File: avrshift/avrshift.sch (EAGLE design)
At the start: 49 parts, among them IC1 AT90S2313P, IC2 7805TV, Q1 BC337-40, Q10 BC337-40, Q11 BC337-40, Q12 BC337-40, Q2 BC337-40, Q3 BC337-40, Q4 BC337-40, Q5 BC337-40, Q6 BC337-40, Q7 BC337-40, Q8 BC337-40, Q9 BC337-40

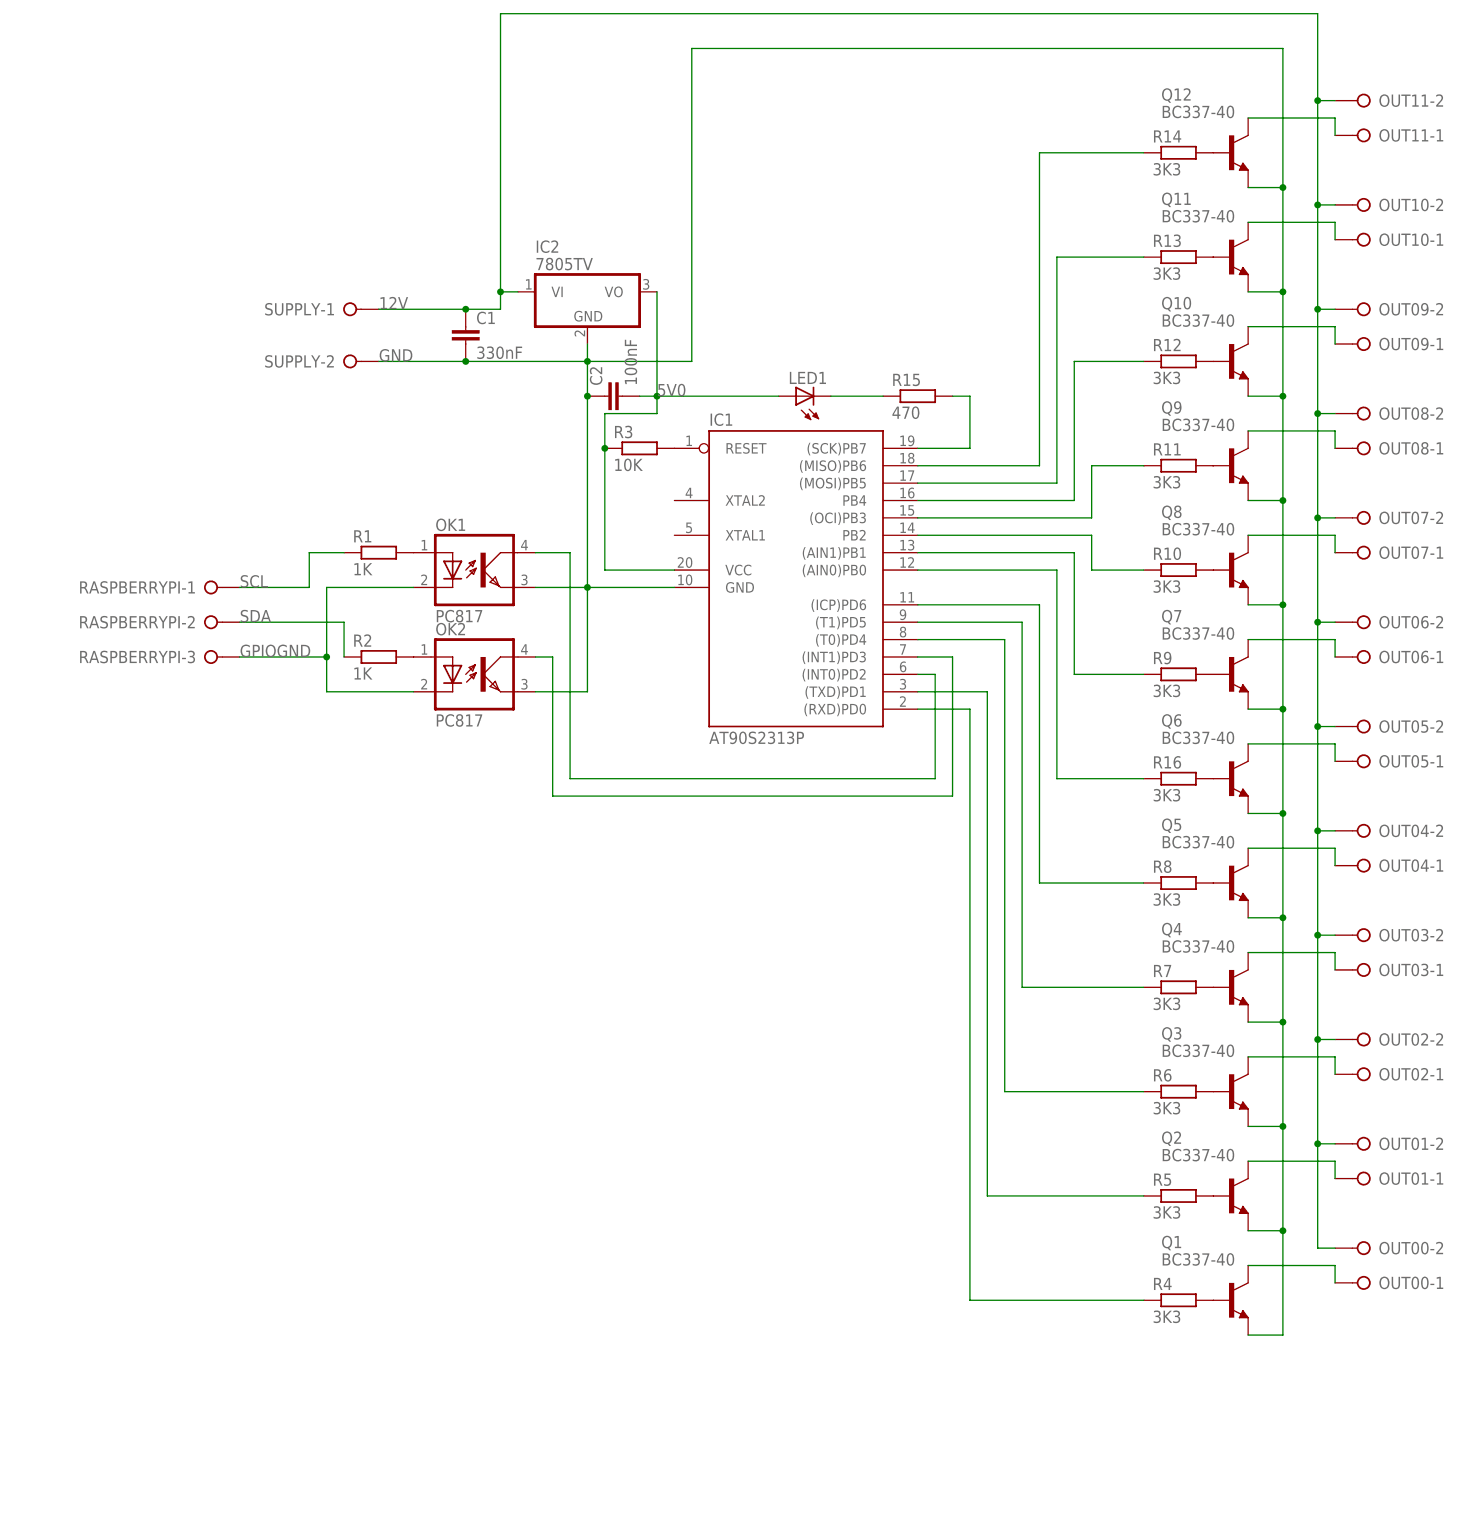
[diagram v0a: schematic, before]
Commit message: avrshift: update schematic, add board layout
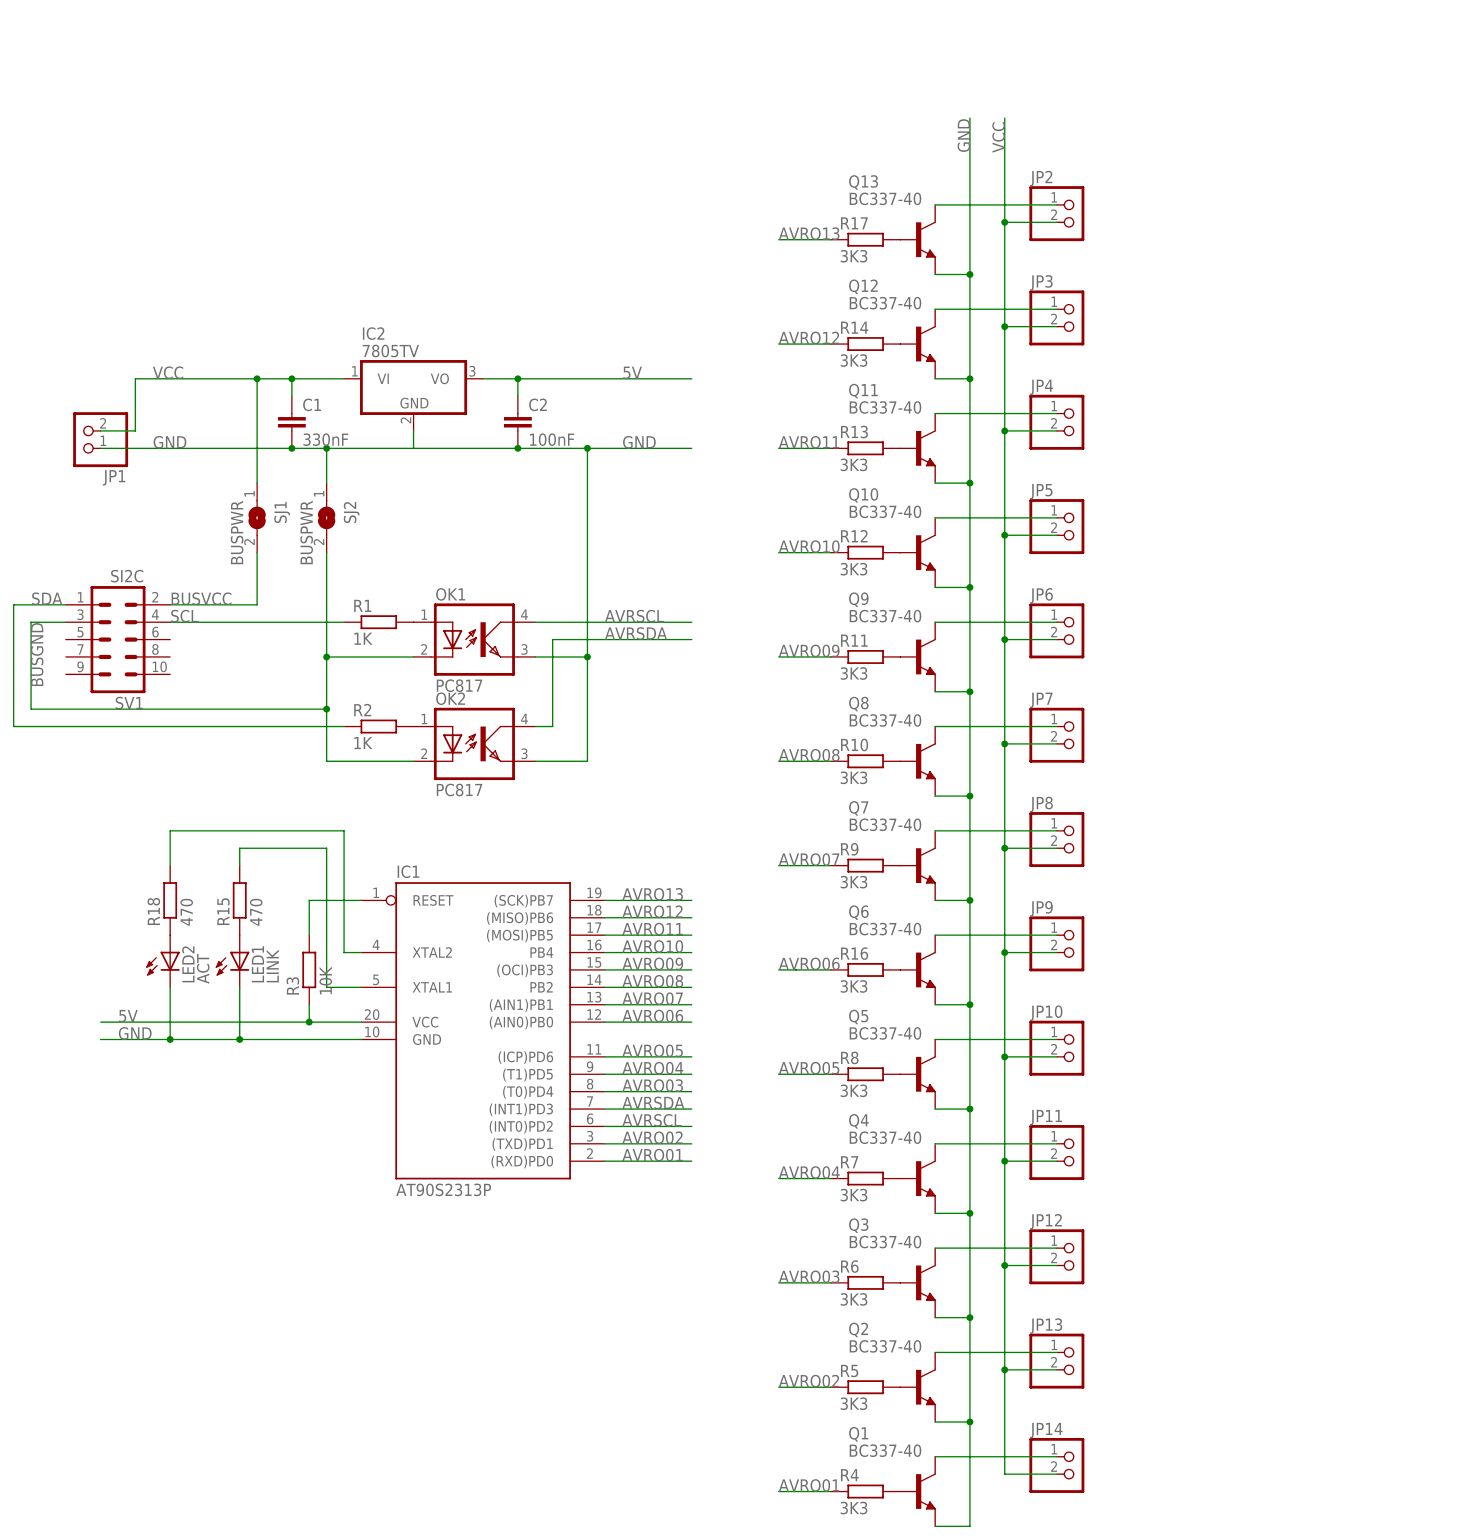
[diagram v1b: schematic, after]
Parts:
- removed OUT00, OUT01, OUT02, OUT03, OUT04, OUT05, OUT06, OUT07, OUT08, OUT09, OUT10, OUT11, SUPPLY: (no value), con-wago-508:W237-02P
- removed RASPBERRYPI: (no value), con-wago-508:W237-3E
- added JP1, JP10, JP11, JP12, JP13, JP14, JP2, JP3, JP4, JP5, JP6, JP7, JP8, JP9: (no value), pinhead:PINHD-1X2
- added LED2: ACT, led:LED3MM
- added Q13: BC337-40, transistor-npn:BC337-40
- added R17: 3K3, resistor:R-EU_0207/10
- added R18: 470, resistor:R-EU_0207/10
- added SJ1, SJ2: BUSPWR, jumper:SJ
- added SV1: SI2C, con-harting-ml:ML10
- LED1: value (none) -> LINK
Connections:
- net N$10 renamed AVRSCL
- net N$23 renamed AVRO01
- net N$24 renamed AVRO02
- net N$25 renamed AVRO03
- net N$26 renamed AVRO04
- net N$27 renamed AVRO05
- net N$28 renamed AVRO06
- net N$29 renamed AVRO07
- net N$30 renamed AVRO08
- net N$31 renamed AVRO09
- net N$32 renamed AVRO10
- net N$33 renamed AVRO11
- net N$34 renamed AVRO12
- net N$8 renamed AVRSDA
- removed net 12V: C1.1, IC2.VI, OUT00-2.KL, OUT01-2.KL, OUT02-2.KL, OUT03-2.KL, OUT04-2.KL, OUT05-2.KL, OUT06-2.KL, OUT07-2.KL, OUT08-2.KL, OUT09-2.KL, OUT10-2.KL, OUT11-2.KL, SUPPLY-1.KL
- removed net 5V0: C2.2, IC1.VCC, IC2.VO, LED1.A, R3.1
- removed net GPIOGND: OK1.C, OK2.C, RASPBERRYPI-3.KL
- removed net N$35: IC1.(SCK)PB7, R15.2
- removed net N$38: OUT01-1.KL, Q2.C
- removed net N$48: OUT11-1.KL, Q12.C
- new net 5V: C2.1, IC1.VCC, IC2.VO, R3.1
- new net AVRO13: IC1.(SCK)PB7, R17.1
- new net BUSGND: OK1.C, OK2.C, SJ2.2, SV1.3
- new net BUSVCC: SJ1.2, SV1.2
- new net N$10: LED1.A, R15.1
- new net N$23: JP3.1, Q12.C
- new net N$33: IC1.XTAL1, R15.2
- new net N$5: Q13.B, R17.2
- new net N$6: JP13.1, Q2.C
- new net N$7: JP2.1, Q13.C
- new net N$8: LED2.A, R18.1
- new net VCC: C1.1, IC2.VI, JP1.2, JP10.2, JP11.2, JP12.2, JP13.2, JP14.2, JP2.2, JP3.2, JP4.2, JP5.2, JP6.2, JP7.2, JP8.2, JP9.2, SJ1.1
- net GND: now also C2.2, JP1.1, LED1.C, LED2.C, Q13.E, SJ2.1; no longer C2.1, SUPPLY-2.KL
- net N$21: now also IC1.XTAL2, R18.2; no longer LED1.C, R15.1
- net N$37: now also JP14.1; no longer OUT00-1.KL
- net N$39: now also JP12.1; no longer OUT02-1.KL
- net N$40: now also JP11.1; no longer OUT03-1.KL
- net N$41: now also JP10.1; no longer OUT04-1.KL
- net N$42: now also JP9.1; no longer OUT05-1.KL
- net N$43: now also JP8.1; no longer OUT06-1.KL
- net N$44: now also JP7.1; no longer OUT07-1.KL
- net N$45: now also JP6.1; no longer OUT08-1.KL
- net N$46: now also JP5.1; no longer OUT09-1.KL
- net N$47: now also JP4.1; no longer OUT10-1.KL
- net SCL: now also SV1.4; no longer RASPBERRYPI-1.KL
- net SDA: now also SV1.1; no longer RASPBERRYPI-2.KL
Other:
- moved on the sheet: C1, C2, IC1, IC2, LED1, OK1, OK2, Q1, Q10, Q11, Q12, Q2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

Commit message: avrshift: schematic/baord bugfixes
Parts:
- LED1: value LINK -> PWR
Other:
- note added: "disconnected: use power supply on JP1 connected: use bus power. JP1 not populated"
- moved on the sheet: SJ1, SJ2
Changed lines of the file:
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@@
 <grid distance="0.1" unitdist="inch" unit="inch" style="lines" multiple="1" display="no" altdistance="0.01" altunitdist="inch" altunit="inch"/>
 <layers>
-<layer number="1" name="Top" color="4" fill="1" visible="yes" active="no"/>
-<layer number="16" name="Bottom" color="1" fill="1" visible="yes" active="no"/>
-<layer number="17" name="Pads" color="2" fill="1" visible="yes" active="no"/>
-<layer number="18" name="Vias" color="2" fill="1" visible="yes" active="no"/>
-<layer number="19" name="Unrouted" color="6" fill="1" visible="yes" active="no"/>
-<layer number="20" name="Dimension" color="15" fill="1" visible="yes" active="no"/>
-<layer number="21" name="tPlace" color="7" fill="1" visible="yes" active="no"/>
-<layer number="22" name="bPlace" color="7" fill="1" visible="yes" active="no"/>
-<layer number="23" name="tOrigins" color="15" fill="1" visible="yes" active="no"/>
-<layer number="24" name="bOrigins" color="15" fill="1" visible="yes" active="no"/>
-<layer number="25" name="tNames" color="7" fill="1" visible="yes" active="no"/>
-<layer number="26" name="bNames" color="7" fill="1" visible="yes" active="no"/>
-<layer number="27" name="tValues" color="7" fill="1" visible="yes" active="no"/>
-<layer number="28" name="bValues" color="7" fill="1" visible="yes" active="no"/>
+<layer number="1" name="Top" color="4" fill="1" visible="no" active="no"/>
+<layer number="16" name="Bottom" color="1" fill="1" visible="no" active="no"/>
+<layer number="17" name="Pads" color="2" fill="1" visible="no" active="no"/>
+<layer number="18" name="Vias" color="2" fill="1" visible="no" active="no"/>
+<layer number="19" name="Unrouted" color="6" fill="1" visible="no" active="no"/>
+<layer number="20" name="Dimension" color="15" fill="1" visible="no" active="no"/>
+<layer number="21" name="tPlace" color="7" fill="1" visible="no" active="no"/>
+<layer number="22" name="bPlace" color="7" fill="1" visible="no" active="no"/>
+<layer number="23" name="tOrigins" color="15" fill="1" visible="no" active="no"/>
+<layer number="24" name="bOrigins" color="15" fill="1" visible="no" active="no"/>
+<layer number="25" name="tNames" color="7" fill="1" visible="no" active="no"/>
+<layer number="26" name="bNames" color="7" fill="1" visible="no" active="no"/>
+<layer number="27" name="tValues" color="7" fill="1" visible="no" active="no"/>
+<layer number="28" name="bValues" color="7" fill="1" visible="no" active="no"/>
 <layer number="29" name="tStop" color="7" fill="3" visible="no" active="no"/>
 <layer number="30" name="bStop" color="7" fill="6" visible="no" active="no"/>
@@
 <layer number="35" name="tGlue" color="7" fill="4" visible="no" active="no"/>
 <layer number="36" name="bGlue" color="7" fill="5" visible="no" active="no"/>
-<layer number="37" name="tTest" color="7" fill="1" visible="yes" active="no"/>
-<layer number="38" name="bTest" color="7" fill="1" visible="yes" active="no"/>
+<layer number="37" name="tTest" color="7" fill="1" visible="no" active="no"/>
+<layer number="38" name="bTest" color="7" fill="1" visible="no" active="no"/>
 <layer number="39" name="tKeepout" color="4" fill="11" visible="no" active="no"/>
 <layer number="40" name="bKeepout" color="1" fill="11" visible="no" active="no"/>
@@
 <layer number="44" name="Drills" color="7" fill="1" visible="no" active="no"/>
 <layer number="45" name="Holes" color="7" fill="1" visible="no" active="no"/>
-<layer number="46" name="Milling" color="3" fill="1" visible="yes" active="no"/>
-<layer number="47" name="Measures" color="7" fill="1" visible="yes" active="no"/>
-<layer number="48" name="Document" color="7" fill="1" visible="yes" active="no"/>
-<layer number="49" name="Reference" color="7" fill="1" visible="yes" active="no"/>
-<layer number="51" name="tDocu" color="6" fill="9" visible="yes" active="no"/>
-<layer number="52" name="bDocu" color="7" fill="1" visible="yes" active="no"/>
+<layer number="46" name="Milling" color="3" fill="1" visible="no" active="no"/>
+<layer number="47" name="Measures" color="7" fill="1" visible="no" active="no"/>
+<layer number="48" name="Document" color="7" fill="1" visible="no" active="no"/>
+<layer number="49" name="Reference" color="7" fill="1" visible="no" active="no"/>
+<layer number="51" name="tDocu" color="6" fill="9" visible="no" active="no"/>
+<layer number="52" name="bDocu" color="7" fill="1" visible="no" active="no"/>
 <layer number="91" name="Nets" color="2" fill="1" visible="yes" active="yes"/>
 <layer number="92" name="Busses" color="1" fill="1" visible="yes" active="yes"/>
@@
 <part name="R15" library="resistor" deviceset="R-EU_" device="0207/10" value="470"/>
 <part name="R18" library="resistor" deviceset="R-EU_" device="0207/10" value="470"/>
-<part name="LED1" library="led" deviceset="LED" device="3MM" value="LINK"/>
+<part name="LED1" library="led" deviceset="LED" device="3MM" value="PWR"/>
 <part name="LED2" library="led" deviceset="LED" device="3MM" value="ACT"/>
 <part name="JP1" library="pinhead" deviceset="PINHD-1X2" device=""/>
@@
 <sheet>
 <plain>
+<text x="-25.4" y="58.42" size="1.778" layer="97">disconnected:
+use power supply on JP1
+connected:
+use bus power. JP1 not populated</text>
 </plain>
 <instances>
@@
 <instance part="Q13" gate="G$1" x="63.5" y="109.22"/>
 <instance part="R17" gate="G$1" x="55.88" y="109.22"/>
-<instance part="SJ1" gate="1" x="-33.02" y="68.58" rot="R270"/>
+<instance part="SJ1" gate="1" x="-35.56" y="71.12" rot="R270"/>
 <instance part="SV1" gate="G$1" x="-53.34" y="50.8" rot="R180"/>
-<instance part="SJ2" gate="1" x="-22.86" y="68.58" rot="R270"/>
+<instance part="SJ2" gate="1" x="-25.4" y="71.12" rot="R270"/>
 <instance part="R3" gate="G$1" x="-25.4" y="2.54" rot="R90"/>
 <instance part="R15" gate="G$1" x="-35.56" y="12.7" rot="R90"/>
@@
 <wire x1="-10.16" y1="78.74" x2="-10.16" y2="81.28" width="0.1524" layer="91"/>
 <pinref part="C1" gate="G$1" pin="2"/>
-<wire x1="-27.94" y1="78.74" x2="-22.86" y2="78.74" width="0.1524" layer="91"/>
+<wire x1="-27.94" y1="78.74" x2="-25.4" y2="78.74" width="0.1524" layer="91"/>
 <pinref part="C2" gate="G$1" pin="2"/>
-<wire x1="-22.86" y1="78.74" x2="-10.16" y2="78.74" width="0.1524" layer="91"/>
+<wire x1="-25.4" y1="78.74" x2="-10.16" y2="78.74" width="0.1524" layer="91"/>
 <wire x1="-10.16" y1="78.74" x2="5.08" y2="78.74" width="0.1524" layer="91"/>
 <wire x1="-55.88" y1="78.74" x2="-27.94" y2="78.74" width="0.1524" layer="91"/>
@@
 <junction x="15.24" y="78.74"/>
 <label x="-48.26" y="78.74" size="1.778" layer="95"/>
-<junction x="-22.86" y="78.74"/>
+<junction x="-25.4" y="78.74"/>
 <pinref part="SJ2" gate="1" pin="1"/>
-<wire x1="-22.86" y1="73.66" x2="-22.86" y2="78.74" width="0.1524" layer="91"/>
+<wire x1="-25.4" y1="76.2" x2="-25.4" y2="78.74" width="0.1524" layer="91"/>
 <label x="20.32" y="78.74" size="1.778" layer="95"/>
 <junction x="5.08" y="78.74"/>
 <pinref part="JP1" gate="G$1" pin="1"/>
+<junction x="-10.16" y="78.74"/>
 </segment>
 <segment>
@@
 <net name="BUSGND" class="0">
 <segment>
-<wire x1="-10.16" y1="48.26" x2="-22.86" y2="48.26" width="0.1524" layer="91"/>
+<wire x1="-10.16" y1="48.26" x2="-25.4" y2="48.26" width="0.1524" layer="91"/>
 <pinref part="OK1" gate="A" pin="C"/>
 <pinref part="SJ2" gate="1" pin="2"/>
-<wire x1="-22.86" y1="48.26" x2="-22.86" y2="63.5" width="0.1524" layer="91"/>
+<wire x1="-25.4" y1="48.26" x2="-25.4" y2="66.04" width="0.1524" layer="91"/>
 <wire x1="-66.04" y1="53.34" x2="-66.04" y2="40.64" width="0.1524" layer="91"/>
 <pinref part="SV1" gate="G$1" pin="3"/>
@@
 <label x="-66.04" y="53.34" size="1.778" layer="95" rot="R270"/>
 <pinref part="OK2" gate="A" pin="C"/>
-<wire x1="-10.16" y1="33.02" x2="-22.86" y2="33.02" width="0.1524" layer="91"/>
-<wire x1="-22.86" y1="40.64" x2="-22.86" y2="33.02" width="0.1524" layer="91"/>
-<wire x1="-66.04" y1="40.64" x2="-22.86" y2="40.64" width="0.1524" layer="91"/>
-<wire x1="-22.86" y1="40.64" x2="-22.86" y2="48.26" width="0.1524" layer="91"/>
-<junction x="-22.86" y="48.26"/>
-<junction x="-22.86" y="40.64"/>
+<wire x1="-10.16" y1="33.02" x2="-25.4" y2="33.02" width="0.1524" layer="91"/>
+<wire x1="-25.4" y1="40.64" x2="-25.4" y2="33.02" width="0.1524" layer="91"/>
+<wire x1="-66.04" y1="40.64" x2="-25.4" y2="40.64" width="0.1524" layer="91"/>
+<wire x1="-25.4" y1="40.64" x2="-25.4" y2="48.26" width="0.1524" layer="91"/>
+<junction x="-25.4" y="48.26"/>
+<junction x="-25.4" y="40.64"/>
 </segment>
 </net>
@@
 <wire x1="-27.94" y1="88.9" x2="-20.32" y2="88.9" width="0.1524" layer="91"/>
 <wire x1="-27.94" y1="86.36" x2="-27.94" y2="88.9" width="0.1524" layer="91"/>
-<wire x1="-33.02" y1="88.9" x2="-27.94" y2="88.9" width="0.1524" layer="91"/>
+<wire x1="-35.56" y1="88.9" x2="-27.94" y2="88.9" width="0.1524" layer="91"/>
 <pinref part="SJ1" gate="1" pin="1"/>
-<wire x1="-33.02" y1="73.66" x2="-33.02" y2="88.9" width="0.1524" layer="91"/>
-<wire x1="-50.8" y1="88.9" x2="-33.02" y2="88.9" width="0.1524" layer="91"/>
-<junction x="-33.02" y="88.9"/>
+<wire x1="-35.56" y1="76.2" x2="-35.56" y2="88.9" width="0.1524" layer="91"/>
+<wire x1="-50.8" y1="88.9" x2="-35.56" y2="88.9" width="0.1524" layer="91"/>
+<junction x="-35.56" y="88.9"/>
 <label x="-48.26" y="88.9" size="1.778" layer="95"/>
 <junction x="-27.94" y="88.9"/>
@@
 <segment>
 <pinref part="SV1" gate="G$1" pin="2"/>
-<wire x1="-45.72" y1="55.88" x2="-33.02" y2="55.88" width="0.1524" layer="91"/>
+<wire x1="-45.72" y1="55.88" x2="-35.56" y2="55.88" width="0.1524" layer="91"/>
 <pinref part="SJ1" gate="1" pin="2"/>
-<wire x1="-33.02" y1="55.88" x2="-33.02" y2="63.5" width="0.1524" layer="91"/>
+<wire x1="-35.56" y1="55.88" x2="-35.56" y2="66.04" width="0.1524" layer="91"/>
 <label x="-45.72" y="55.88" size="1.778" layer="95"/>
 </segment>
@@
 </schematic>
 </drawing>
+<compatibility>
+<note version="6.3" minversion="6.2.2" severity="warning">
+Since Version 6.2.2 text objects can contain more than one line,
+which will not be processed correctly with this version.
+</note>
+</compatibility>
 </eagle>

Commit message: moar eagle
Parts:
- JP1: value (none) -> PWR
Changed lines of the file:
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@@
 <part name="LED1" library="led" deviceset="LED" device="3MM" value="PWR"/>
 <part name="LED2" library="led" deviceset="LED" device="3MM" value="ACT"/>
-<part name="JP1" library="pinhead" deviceset="PINHD-1X2" device=""/>
+<part name="JP1" library="pinhead" deviceset="PINHD-1X2" device="" value="PWR"/>
 <part name="JP2" library="pinhead" deviceset="PINHD-1X2" device=""/>
 <part name="JP3" library="pinhead" deviceset="PINHD-1X2" device=""/>
